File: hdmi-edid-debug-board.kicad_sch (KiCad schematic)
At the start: 108 parts, among them J1 HDMI-A_WE_685119134923, J2 PinHeader_2x3_P2.54mm_Drill1.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, J4 HDMI-A_WE_685119134923, J5 USB-C_GCT_USB4105-GF-A, J6 JST_SH_1x4_SM04B-SRSS-TB-LF-SN, J7 PinHeader_2x3_P2.54mm_Drill1.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, Q1 DMG1012T-7, U2 24AA024T-I-SN, U3 NTS0102_TSSOP, U4 TLV70033_SC70, U5 FT4232H_VQFN, U6 TPS2117DRLR, Y1 Oscillator_12MHz_ASFLMB

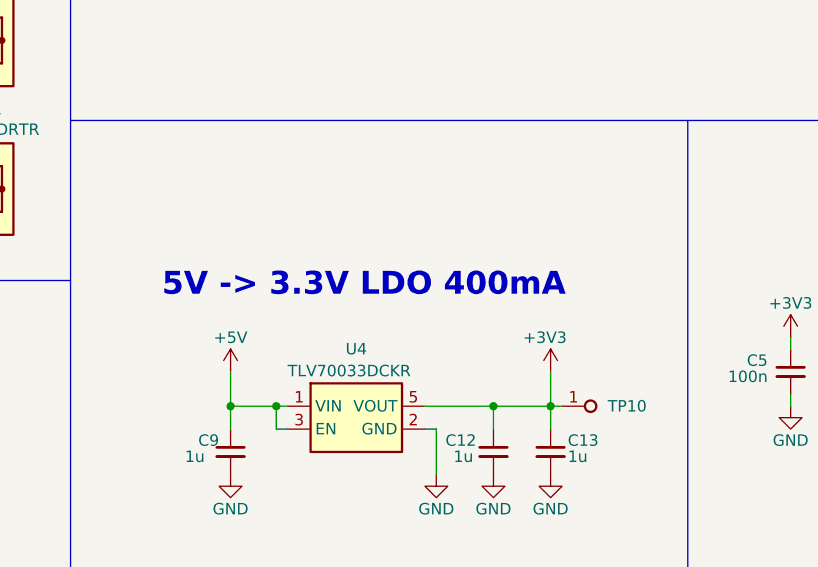
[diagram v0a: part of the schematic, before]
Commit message: [#77796] Update LDO description on schematic
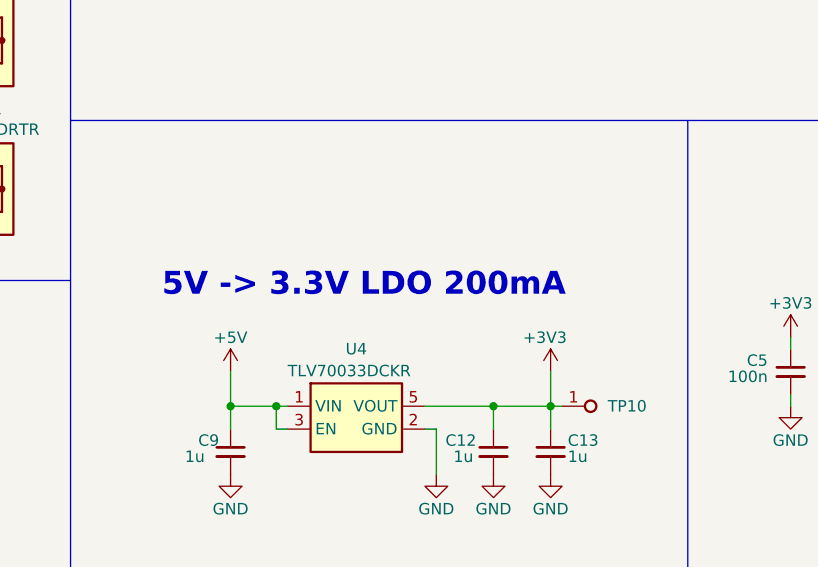
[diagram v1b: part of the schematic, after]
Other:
- note added: "5V -> 3.3V LDO 200mA"
- note removed: "5V -> 3.3V LDO 400mA"
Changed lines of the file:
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@@
 		)
 	)
-	(text "5V -> 3.3V LDO 400mA"
+	(text "5V -> 3.3V LDO 200mA"
 		(exclude_from_sim no)
 		(at 265.43 200.152 0)
